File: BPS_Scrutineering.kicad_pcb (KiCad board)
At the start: 2 copper layers, 38.7 x 59.1 mm, 21 parts, among them J1 Conn_01x07_Male, J2 Conn_01x07_Male, J3 Conn_01x07_Male, J4 Conn_01x07_Male

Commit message: ready for peer review
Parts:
- R1: value R -> 0
- moved JP16 20.6 mm to (62.2, 87.0), turned to 90 degrees
- moved R1 16.4 mm to (71.1, 87.0), turned to 180 degrees
- moved JP15 2.01 mm to (77.5, 87.0), turned to 90 degrees
- moved J2 1.27 mm to (81.3, 78.7)
- moved J3 1.27 mm to (81.3, 108.0)
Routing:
- net Net-(JP15-Pad1): track 9.57 -> 5.41 mm
- net Net-(J1-Pad7): track 11.6 -> 13.3 mm
- net Net-(JP16-Pad2): track 6.87 -> 5.41 mm
- net Net-(J2-Pad7): track 11.2 -> 9.94 mm
- net Net-(J3-Pad7): track 11.2 -> 9.94 mm
- net Net-(J3-Pad3): track 11.2 -> 9.94 mm
- net Net-(J2-Pad3): track 11.2 -> 9.94 mm
- net Net-(J3-Pad6): track 10.7 -> 9.42 mm
- net Net-(J3-Pad5): track 10.2 -> 8.89 mm
- net Net-(J3-Pad4): track 10.7 -> 9.42 mm
- net Net-(J3-Pad2): track 11.7 -> 10.5 mm
- net Net-(J2-Pad6): track 10.7 -> 9.42 mm
- net Net-(J2-Pad5): track 10.2 -> 8.89 mm
- net Net-(J2-Pad4): track 10.7 -> 9.42 mm
- net Net-(J2-Pad2): track 11.7 -> 10.5 mm
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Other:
- board size 38.7 x 59.1 mm -> 29.8 x 59.1 mm
- board text added: "Fall 2020"

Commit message: Add files via upload
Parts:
- added H1: MountingHole, MountingHole:MountingHole_3mm, F.Cu at (81.9, 116.8)
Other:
- board size 29.8 x 59.1 mm -> 29.8 x 64.8 mm

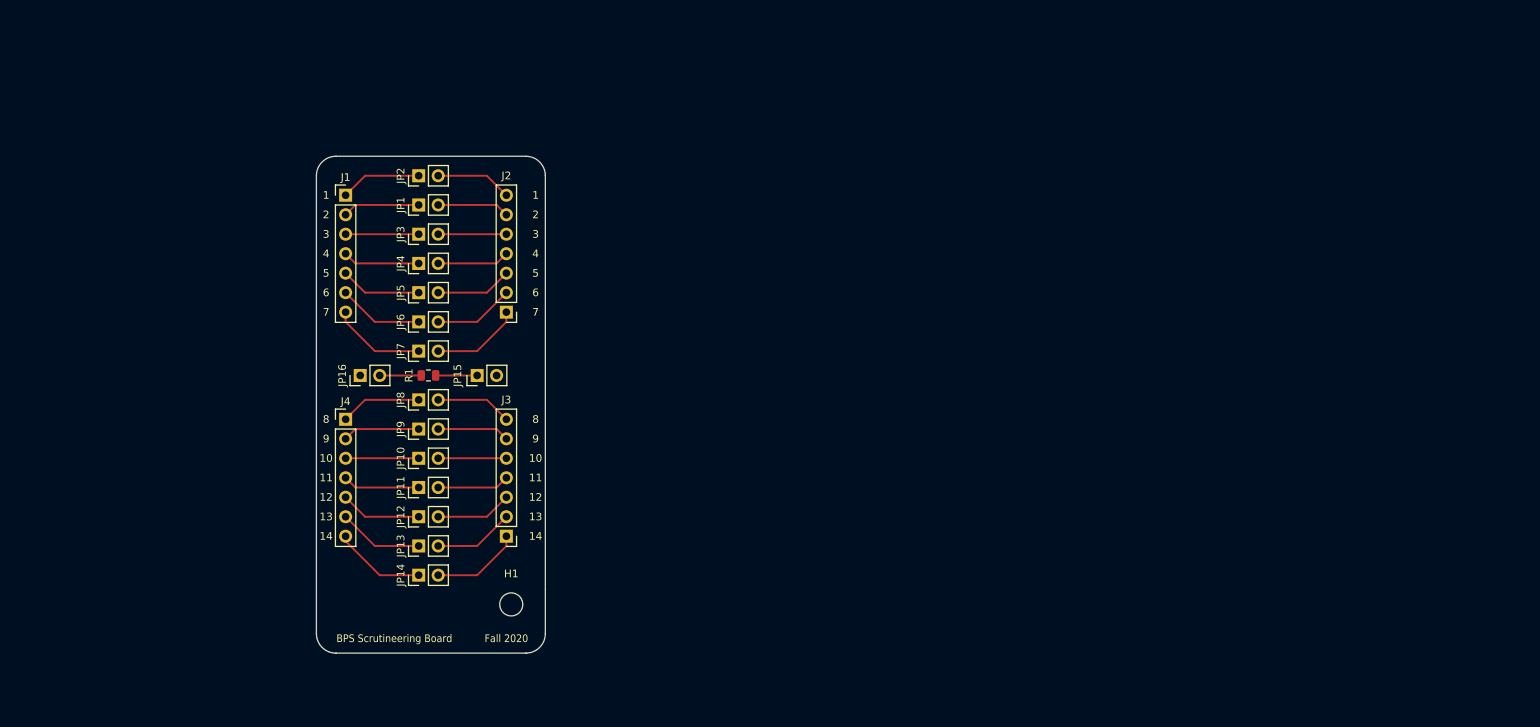
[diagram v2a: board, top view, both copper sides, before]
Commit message: schematic done, editing PCB, number of banana jacks?
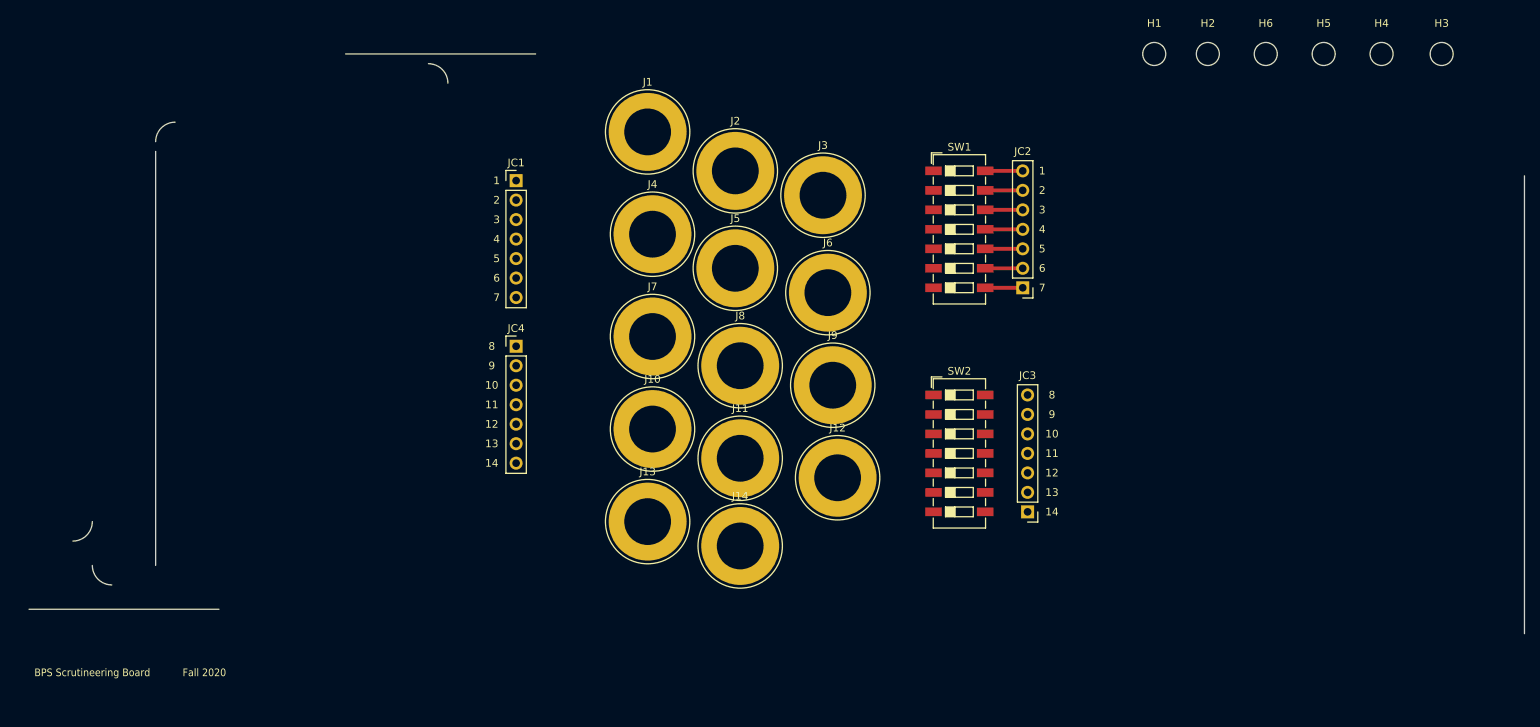
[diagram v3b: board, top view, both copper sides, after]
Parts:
- removed JP1, JP10, JP11, JP12, JP13, JP14, JP15, JP16, JP2, JP3, JP4, JP5, JP6, JP7, JP8, JP9: Jumper, Connector_PinHeader_2.54mm:PinHeader_1x02_P2.54mm_Vertical
- removed R1: 0, Resistor_SMD:R_0805_2012Metric
- added H2: MountingHole, MountingHole:MountingHole_3mm, F.Cu at (172.7, 45.1)
- added H3: MountingHole, MountingHole:MountingHole_3mm, F.Cu at (203.2, 45.1)
- added H4: MountingHole, MountingHole:MountingHole_3mm, F.Cu at (195.4, 45.1)
- added H5: MountingHole, MountingHole:MountingHole_3mm, F.Cu at (187.8, 45.1)
- added H6: MountingHole, MountingHole:MountingHole_3mm, F.Cu at (180.3, 45.1)
- added J1: Conn_01x01_Female, Connector:Banana_Jack_1Pin, F.Cu at (99.7, 55.2)
- added J10: Conn_01x01_Female, Connector:Banana_Jack_1Pin, F.Cu at (100.3, 94.0)
- added J11: Conn_01x01_Female, Connector:Banana_Jack_1Pin, F.Cu at (111.8, 97.8)
- added J12: Conn_01x01_Female, Connector:Banana_Jack_1Pin, F.Cu at (124.5, 100.3)
- added J13: Conn_01x01_Female, Connector:Banana_Jack_1Pin, F.Cu at (99.7, 106.0)
- added J14: Conn_01x01_Female, Connector:Banana_Jack_1Pin, F.Cu at (111.8, 109.2)
- added J2: Conn_01x01_Female, Connector:Banana_Jack_1Pin, F.Cu at (111.1, 60.3)
- added J3: Conn_01x01_Female, Connector:Banana_Jack_1Pin, F.Cu at (122.6, 63.5)
- added J4: Conn_01x01_Female, Connector:Banana_Jack_1Pin, F.Cu at (100.3, 68.6)
- added J5: Conn_01x01_Female, Connector:Banana_Jack_1Pin, F.Cu at (111.1, 73.0)
- added J6: Conn_01x01_Female, Connector:Banana_Jack_1Pin, F.Cu at (123.2, 76.2)
- added J7: Conn_01x01_Female, Connector:Banana_Jack_1Pin, F.Cu at (100.3, 81.9)
- added J8: Conn_01x01_Female, Connector:Banana_Jack_1Pin, F.Cu at (111.8, 85.7)
- added J9: Conn_01x01_Female, Connector:Banana_Jack_1Pin, F.Cu at (123.8, 88.3)
- added SW1: SW_DIP_x07, Button_Switch_SMD:SW_DIP_SPSTx07_Slide_6.7x19.34mm_W6.73mm_P2.54mm_LowProfile_JPin, F.Cu at (140.3, 67.9)
- added SW2: SW_DIP_x07, Button_Switch_SMD:SW_DIP_SPSTx07_Slide_6.7x19.34mm_W6.73mm_P2.54mm_LowProfile_JPin, F.Cu at (140.3, 97.2)
- moved H1 110.3 mm to (165.7, 45.1)
- moved JC3 68.0 mm to (149.2, 104.8)
- moved JC2 67.4 mm to (148.6, 75.6)
- moved JC4 24.2 mm to (82.5, 83.2)
- moved JC1 22.3 mm to (82.5, 61.6)
- renumbered J1 to JC1, J2 to JC2, J3 to JC3, J4 to JC4
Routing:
- net Net-(J7-Pad1): track 13.3 -> 0.00 mm
- net Net-(J14-Pad1): track 12.0 -> 0.00 mm
- net Net-(JC3-Pad1): track 11.7 -> 0.00 mm
- net Net-(J8-Pad1): track 11.2 -> 0.00 mm
- net Net-(J6-Pad1): track 11.1 -> 0.00 mm
- net Net-(J13-Pad1): track 11.1 -> 0.00 mm
- net Net-(J5-Pad1): track 10.6 -> 0.00 mm
- net Net-(J1-Pad1): track 10.6 -> 0.00 mm
- net Net-(J12-Pad1): track 10.6 -> 0.00 mm
- net Net-(JC3-Pad2): track 10.5 -> 0.00 mm
- net Net-(J2-Pad1): track 10.1 -> 0.00 mm
- net Net-(J9-Pad1): track 10.1 -> 0.00 mm
- net Net-(J4-Pad1): track 10.1 -> 0.00 mm
- net Net-(J11-Pad1): track 10.1 -> 0.00 mm
- net Net-(JC3-Pad7): track 9.94 -> 0.00 mm
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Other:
- board size 29.8 x 64.8 mm -> 194.9 x 75.6 mm

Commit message: finished PCB
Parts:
- moved H6 113.1 mm to (83.8, 104.1)
- moved H2 95.3 mm to (83.8, 79.4)
- moved H1 81.8 mm to (84.5, 54.6)
- moved H3 78.1 mm to (153.7, 105.4)
- moved H4 53.5 mm to (154.3, 79.4)
- moved H5 35.5 mm to (153.7, 54.6)
- moved J14 22.9 mm to (134.6, 108.6)
- moved JC4 7.65 mm to (90.2, 82.5)
- moved JC1 7.65 mm to (90.2, 61.0)
- moved JC3 6.63 mm to (147.3, 98.4)
- moved SW2 6.48 mm to (139.1, 90.8)
- moved J13 2.01 mm to (97.8, 106.7)
- moved JC2 1.27 mm to (147.3, 75.6)
- moved SW1 1.27 mm to (139.1, 67.9)
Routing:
- net Net-(J10-Pad1): track 0.00 -> 62.6 mm
- net Net-(J8-Pad1): track 0.00 -> 62.3 mm
- net Net-(J14-Pad1): track 0.00 -> 61.1 mm
- net Net-(J13-Pad1): track 0.00 -> 60.3 mm
- net Net-(J11-Pad1): track 0.00 -> 59.1 mm
- net Net-(J12-Pad1): track 0.00 -> 54.0 mm
- net Net-(J2-Pad1): track 0.00 -> 52.1 mm
- net Net-(J7-Pad1): track 0.00 -> 51.6 mm
- net Net-(J1-Pad1): track 0.00 -> 51.2 mm
- net Net-(J9-Pad1): track 0.00 -> 50.3 mm
- net Net-(J6-Pad1): track 0.00 -> 49.7 mm
- net Net-(J3-Pad1): track 0.00 -> 49.5 mm
- net Net-(J5-Pad1): track 0.00 -> 48.2 mm
- net Net-(J4-Pad1): track 0.00 -> 46.9 mm
- net Net-(JC3-Pad7): track 0.00 -> 4.89 mm
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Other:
- board size 194.9 x 75.6 mm -> 77.5 x 64.8 mm

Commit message: Finished PCB
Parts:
- removed H1, H2, H3, H4, H5, H6: MountingHole, MountingHole:MountingHole_3mm
- added LOGO1: Logo_Placeholder, UTSVT_Special:UTSVT_Logo_Symbol, F.Cu at (85.1, 124.5)
- added LOGO2: Logo_Placeholder, UTSVT_Special:Hallock_Image, B.Cu at (139.7, 106.7)
- moved J14 28.3 mm to (106.7, 113.0)
- moved JC1 15.2 mm to (74.9, 61.0)
- moved JC4 15.2 mm to (74.9, 82.5)
- moved J3 11.4 mm to (121.9, 52.1)
- moved JC2 11.4 mm to (158.8, 75.6)
- moved JC3 11.4 mm to (158.8, 98.4)
- moved J10 9.67 mm to (91.4, 97.8)
- moved J2 9.38 mm to (106.7, 52.1)
- moved J13 8.98 mm to (91.4, 113.0)
- moved J4 8.98 mm to (91.4, 67.3)
- moved J6 8.98 mm to (121.9, 67.3)
- moved J7 8.91 mm to (91.4, 82.5)
- moved J1 8.84 mm to (91.4, 52.1)
- moved J5 7.24 mm to (106.7, 67.3)
- moved J9 6.02 mm to (121.9, 82.5)
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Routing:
- net Net-(J3-Pad1): track 49.5 -> 72.8 mm, vias 0 -> 1
- net Net-(J1-Pad1): track 51.2 -> 73.8 mm
- net Net-(J4-Pad1): track 46.9 -> 66.0 mm
- net Net-(J5-Pad1): track 48.2 -> 66.9 mm, vias 0 -> 2
- net Net-(J2-Pad1): track 52.1 -> 70.0 mm
- net Net-(J6-Pad1): track 49.7 -> 65.8 mm
- net Net-(J13-Pad1): track 60.3 -> 76.0 mm
- net Net-(J9-Pad1): track 50.3 -> 65.9 mm
- net Net-(J12-Pad1): track 54.0 -> 69.6 mm
- net Net-(J7-Pad1): track 51.6 -> 66.3 mm
- net Net-(J11-Pad1): track 59.1 -> 71.6 mm, vias 0 -> 2
- net Net-(J14-Pad1): track 61.1 -> 73.1 mm
- net Net-(JC3-Pad7): track 4.89 -> 16.3 mm
- net Net-(JC3-Pad6): track 4.89 -> 16.3 mm
- net Net-(JC3-Pad5): track 4.89 -> 16.3 mm
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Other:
- board size 77.5 x 64.8 mm -> 97.8 x 90.2 mm
- board text added: "UTSVT - BPS Scrutineering v1.0 Fall 2020"
- board text removed: "BPS Scrutineering Board"
- board text removed: "Fall 2020"

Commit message: PCB finished
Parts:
- JC1, JC2, JC3, JC4: value Conn_01x07_Male -> Conn_01x07; footprint Connector_PinHeader_2.54mm:PinHeader_1x07_P2.54mm_Vertical -> Connector_Molex:Molex_Micro-Fit_3.0_43650-0700_1x07_P3.00mm_Horizontal
- moved JC4 19.3 mm to (82.5, 100.3), turned to 90 degrees
- moved JC2 16.5 mm to (151.1, 61.0), turned to 270 degrees
- moved JC1 14.8 mm to (82.5, 73.7), turned to 90 degrees
- moved JC3 13.2 mm to (151.1, 87.6), turned to 270 degrees
- renumbered LOGO2 to Dr_Hallock1, LOGO1 to UTSVT_Logo1
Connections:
- JC1 pad 1: Net-(J1-Pad1) -> Net-(J7-Pad1)
- JC1 pad 2: Net-(J2-Pad1) -> Net-(J6-Pad1)
- JC1 pad 3: Net-(J3-Pad1) -> Net-(J5-Pad1)
- JC1 pad 5: Net-(J5-Pad1) -> Net-(J3-Pad1)
- JC1 pad 6: Net-(J6-Pad1) -> Net-(J2-Pad1)
- JC1 pad 7: Net-(J7-Pad1) -> Net-(J1-Pad1)
- JC4 pad 1: Net-(J8-Pad1) -> Net-(J14-Pad1)
- JC4 pad 2: Net-(J9-Pad1) -> Net-(J13-Pad1)
- JC4 pad 3: Net-(J10-Pad1) -> Net-(J12-Pad1)
- JC4 pad 5: Net-(J12-Pad1) -> Net-(J10-Pad1)
- JC4 pad 6: Net-(J13-Pad1) -> Net-(J9-Pad1)
- JC4 pad 7: Net-(J14-Pad1) -> Net-(J8-Pad1)
- SW1 pad 10: Net-(JC2-Pad3) -> Net-(JC2-Pad5)
- SW1 pad 12: Net-(JC2-Pad5) -> Net-(JC2-Pad3)
- SW1 pad 13: Net-(JC2-Pad6) -> Net-(JC2-Pad2)
- SW1 pad 14: Net-(JC2-Pad7) -> Net-(JC2-Pad1)
- SW1 pad 8: Net-(JC2-Pad1) -> Net-(JC2-Pad7)
- SW1 pad 9: Net-(JC2-Pad2) -> Net-(JC2-Pad6)
- SW2 pad 10: Net-(JC3-Pad3) -> Net-(JC3-Pad5)
- SW2 pad 12: Net-(JC3-Pad5) -> Net-(JC3-Pad3)
- SW2 pad 13: Net-(JC3-Pad6) -> Net-(JC3-Pad2)
- SW2 pad 14: Net-(JC3-Pad7) -> Net-(JC3-Pad1)
- SW2 pad 8: Net-(JC3-Pad1) -> Net-(JC3-Pad7)
- SW2 pad 9: Net-(JC3-Pad2) -> Net-(JC3-Pad6)
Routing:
- net Net-(J11-Pad1): track 71.6 -> 58.8 mm, vias 2 -> 0
- net Net-(J2-Pad1): track 70.0 -> 60.4 mm, vias 0 -> 1
- net Net-(J14-Pad1): track 73.1 -> 64.5 mm
- net Net-(J10-Pad1): track 68.9 -> 61.3 mm, vias 0 -> 2
- net Net-(JC2-Pad1): track 16.3 -> 8.96 mm
- net Net-(JC2-Pad2): track 16.3 -> 9.15 mm
- net Net-(JC2-Pad3): track 16.3 -> 9.34 mm
- net Net-(J4-Pad1): track 66.0 -> 59.2 mm, vias 0 -> 1
- net Net-(JC2-Pad4): track 16.3 -> 9.53 mm
- net Net-(JC2-Pad5): track 16.3 -> 9.73 mm
- net Net-(J7-Pad1): track 66.3 -> 59.7 mm
- net Net-(JC2-Pad6): track 16.3 -> 9.92 mm
- net Net-(JC2-Pad7): track 16.3 -> 10.1 mm
- net Net-(J1-Pad1): track 73.8 -> 67.8 mm
- net Net-(J3-Pad1): track 72.8 -> 66.9 mm, vias 1 -> 0
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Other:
- board text added: "To BPS Minion Board"
- board text added: "To Batteries"

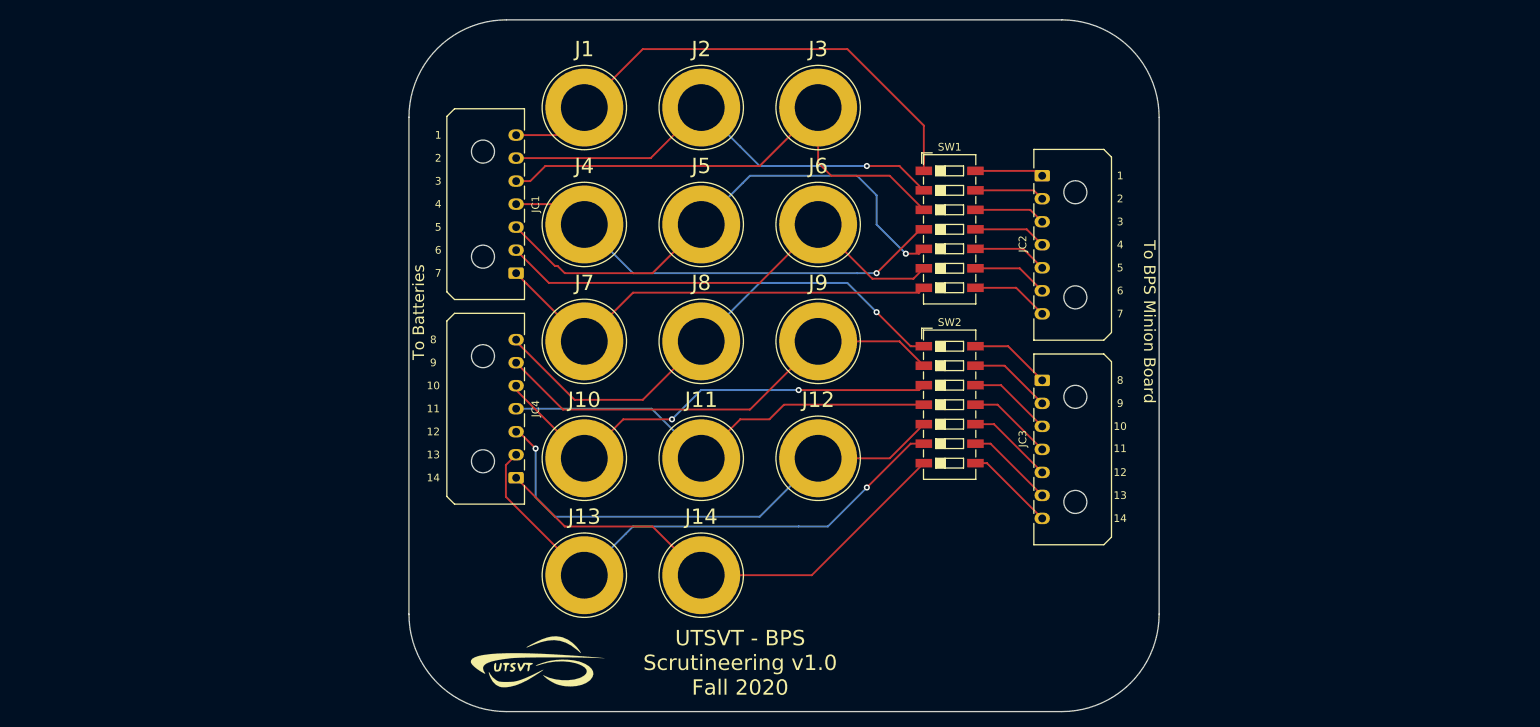
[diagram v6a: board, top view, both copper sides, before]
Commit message: Flipped Connectors
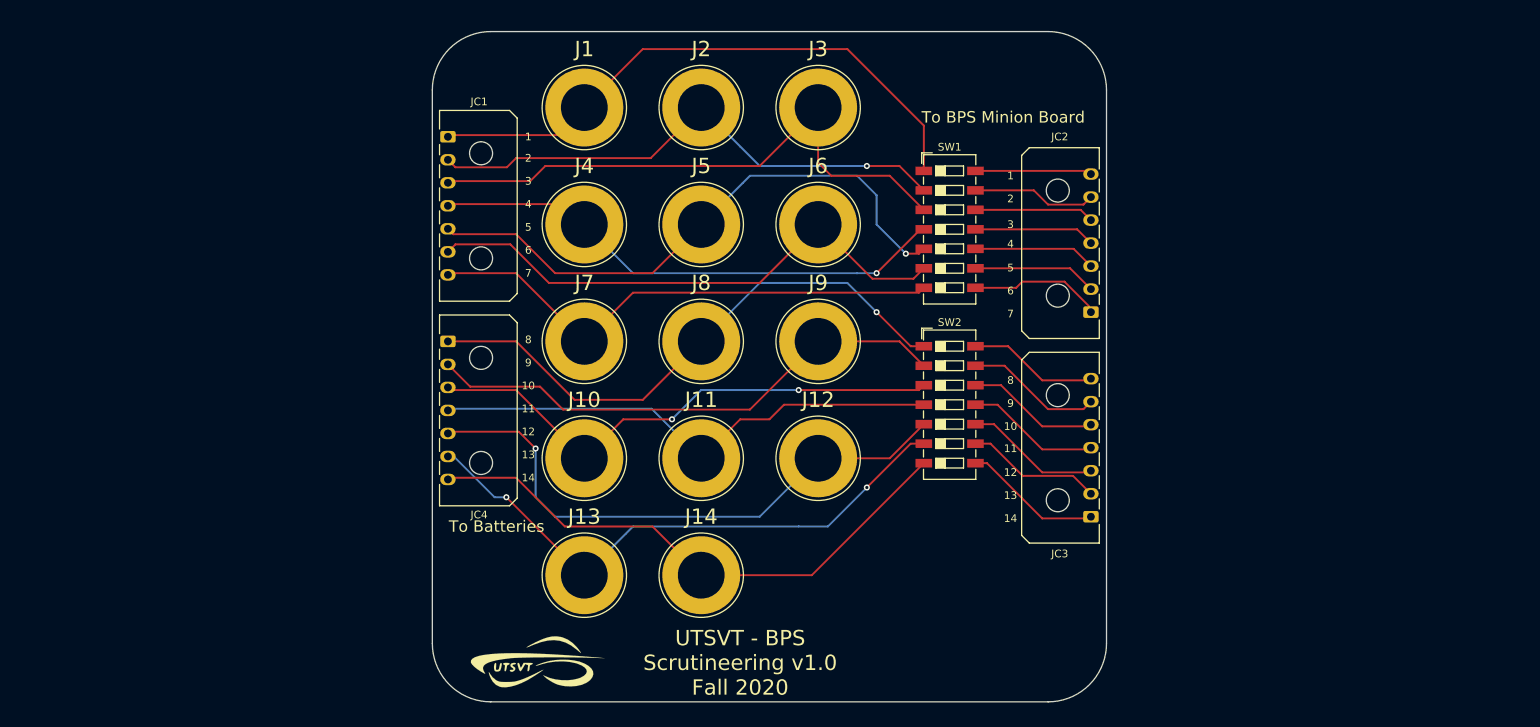
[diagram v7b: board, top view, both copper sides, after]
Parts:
- moved JC4 19.9 mm to (73.7, 82.5), turned to 270 degrees
- moved JC1 19.9 mm to (73.7, 55.9), turned to 270 degrees
- moved JC3 18.9 mm to (157.5, 105.4), turned to 90 degrees
- moved JC2 18.9 mm to (157.5, 78.7), turned to 90 degrees
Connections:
- JC1 pad 1: Net-(J7-Pad1) -> Net-(J1-Pad1)
- JC1 pad 2: Net-(J6-Pad1) -> Net-(J2-Pad1)
- JC1 pad 3: Net-(J5-Pad1) -> Net-(J3-Pad1)
- JC1 pad 5: Net-(J3-Pad1) -> Net-(J5-Pad1)
- JC1 pad 6: Net-(J2-Pad1) -> Net-(J6-Pad1)
- JC1 pad 7: Net-(J1-Pad1) -> Net-(J7-Pad1)
- JC4 pad 1: Net-(J14-Pad1) -> Net-(J8-Pad1)
- JC4 pad 2: Net-(J13-Pad1) -> Net-(J9-Pad1)
- JC4 pad 3: Net-(J12-Pad1) -> Net-(J10-Pad1)
- JC4 pad 5: Net-(J10-Pad1) -> Net-(J12-Pad1)
- JC4 pad 6: Net-(J9-Pad1) -> Net-(J13-Pad1)
- JC4 pad 7: Net-(J8-Pad1) -> Net-(J14-Pad1)
- SW1 pad 10: Net-(JC2-Pad5) -> Net-(JC2-Pad3)
- SW1 pad 12: Net-(JC2-Pad3) -> Net-(JC2-Pad5)
- SW1 pad 13: Net-(JC2-Pad2) -> Net-(JC2-Pad6)
- SW1 pad 14: Net-(JC2-Pad1) -> Net-(JC2-Pad7)
- SW1 pad 8: Net-(JC2-Pad7) -> Net-(JC2-Pad1)
- SW1 pad 9: Net-(JC2-Pad6) -> Net-(JC2-Pad2)
- SW2 pad 10: Net-(JC3-Pad5) -> Net-(JC3-Pad3)
- SW2 pad 12: Net-(JC3-Pad3) -> Net-(JC3-Pad5)
- SW2 pad 13: Net-(JC3-Pad2) -> Net-(JC3-Pad6)
- SW2 pad 14: Net-(JC3-Pad1) -> Net-(JC3-Pad7)
- SW2 pad 8: Net-(JC3-Pad7) -> Net-(JC3-Pad1)
- SW2 pad 9: Net-(JC3-Pad6) -> Net-(JC3-Pad2)
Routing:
- net Net-(J2-Pad1): track 60.4 -> 70.1 mm
- net Net-(J6-Pad1): track 61.6 -> 71.2 mm
- net Net-(J3-Pad1): track 66.9 -> 75.8 mm
- net Net-(J1-Pad1): track 67.8 -> 76.8 mm
- net Net-(J4-Pad1): track 59.2 -> 68.2 mm
- net Net-(J14-Pad1): track 64.5 -> 73.4 mm
- net Net-(J12-Pad1): track 66.5 -> 75.4 mm
- net Net-(J7-Pad1): track 59.7 -> 68.7 mm
- net Net-(J11-Pad1): track 58.8 -> 67.7 mm
- net Net-(J5-Pad1): track 67.6 -> 76.4 mm
- net Net-(J9-Pad1): track 60.7 -> 69.5 mm
- net Net-(J8-Pad1): track 66.3 -> 74.9 mm
- net Net-(J10-Pad1): track 61.3 -> 69.8 mm
- net Net-(JC2-Pad1): track 8.96 -> 17.3 mm
- net Net-(JC3-Pad1): track 10.5 -> 18.1 mm
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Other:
- board size 97.8 x 90.2 mm -> 87.9 x 87.4 mm
